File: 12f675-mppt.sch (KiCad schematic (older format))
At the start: 39 parts, among them IC1 PIC12F629-I/P, Q1 BUK9511-55A127, Q2 BUK9511-55A127, Q3 2N2222A, Q4 2N2222A, Q5 2N2907A, SW1 Write OP-AMP DIFF, U1 7805, U2 LM358N

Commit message: add PCB layout.
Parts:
- removed U1: 7805, symbol 12f675-mppt-rescue:7805
- added J1: S+, Connectors:1pin, symbol Connector:Conn_01x01_Male
- added J2: S-, Connectors:1pin, symbol Connector:Conn_01x01_Male
- added J3: O+, Connectors:1pin, symbol Connector:Conn_01x01_Male
- added J4: O-, Connectors:1pin, symbol Connector:Conn_01x01_Male
- added U1: LM7805_TO220, TO_SOT_Packages_THT:TO-220-3_Vertical, symbol Regulator_Linear:LM7805_TO220
- C1, C2, C3, C5, C7: footprint (none) -> Capacitors_THT:CP_Radial_D12.5mm_P5.00mm
- C4: footprint (none) -> Capacitors_THT:C_Disc_D7.5mm_W4.4mm_P5.00mm
- D1, D2, D6: footprint (none) -> Diodes_THT:D_DO-201AD_P15.24mm_Horizontal
- D3, D5: footprint (none) -> Diodes_THT:D_DO-41_SOD81_P10.16mm_Horizontal
- D4, D8, D9: footprint (none) -> LEDs:LED_D4.0mm
- IC1, U2: footprint (none) -> Housings_DIP:DIP-8_W7.62mm_LongPads
- L1: footprint (none) -> Inductors_THT:L_Toroid_Vertical_L33.0mm_W17.8mm_P12.70mm_Pulse_KM-5
- Q1, Q2: footprint (none) -> TO_SOT_Packages_THT:TO-220-3_Vertical
- Q3, Q4, Q5: footprint (none) -> TO_SOT_Packages_THT:TO-92_Inline_Wide
- R1, R10, R12, R13, R14, R15, R16, R2, R3, R4, R5, R6, R7, R8, R9: footprint (none) -> Resistors_THT:R_Axial_DIN0309_L9.0mm_D3.2mm_P12.70mm_Horizontal
- SW1: footprint (none) -> Buttons_Switches_THT:SW_PUSH_6mm
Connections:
- net labels added: +24V, GNDPWR, PRI_HI, PRI_LO
- net labels removed: L+, L-, S+, S-
- wire segments 148 -> 154

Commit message: Fix High-z turn on FET problem.
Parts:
- added R11: 10k, Resistors_THT:R_Axial_DIN0309_L9.0mm_D3.2mm_P12.70mm_Horizontal, symbol Device:R
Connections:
- net BootStrap: now also R11.1
- net at IC1.7 (CIN+/ICSPDAT/GP0), R7.2: now also R11.2
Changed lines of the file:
@@
 Sheet 1 1
 Title "Simple MPPT with 12F675 v5"
-Date "2019-01-11"
-Rev "1.6b"
+Date "2019-02-13"
+Rev "1.61"
 Comp ""
 Comment1 ""
@@
 	5850 2650 5850 2700
 Wire Wire Line
-	5250 3400 5450 3400
+	5250 3400 5300 3400
 Wire Wire Line
 	5450 3400 5450 3300
@@
 Connection ~ 5850 2350
 Wire Wire Line
-	5200 2350 3500 2350
+	5200 2350 5100 2350
 Wire Wire Line
 	6250 2700 6300 2700
@@
 Wire Wire Line
 	1200 1300 1350 1300
+$Comp
+L Device:R R11
+U 1 1 5C640CF9
+P 5100 2800
+F 0 "R11" V 5180 2800 50  0000 C CNN
+F 1 "10k" V 5100 2800 50  0000 C CNN
+F 2 "Resistors_THT:R_Axial_DIN0309_L9.0mm_D3.2mm_P12.70mm_Horizontal" V 5030 2800 30  0001 C CNN
+F 3 "" H 5100 2800 30  0000 C CNN
+	1    5100 2800
+	1    0    0    -1
+$EndComp
+Wire Wire Line
+	5300 3400 5300 2950
+Wire Wire Line
+	5300 2950 5100 2950
+Connection ~ 5300 3400
+Wire Wire Line
+	5300 3400 5450 3400
+Wire Wire Line
+	5100 2350 5100 2650
+Connection ~ 5100 2350
+Wire Wire Line
+	5100 2350 3500 2350
 $EndSCHEMATC

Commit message: Fix R1, R15 values.
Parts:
- R1: value 4.7k -> 10k
- R15: value 10k -> 4.7k
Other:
- note added: "R15 : 6A -> 3.3k"
- note removed: "R15 : 6A -> 4.7k, 3A -> 10k"
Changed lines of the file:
@@
 Sheet 1 1
 Title "Simple MPPT with 12F675 v5"
-Date "2019-02-13"
-Rev "1.61"
+Date "2019-02-15"
+Rev "1.62"
 Comp ""
 Comment1 ""
@@
 P 9200 4850
 F 0 "R1" V 9280 4850 50  0000 C CNN
-F 1 "4.7k" V 9200 4850 50  0000 C CNN
+F 1 "10k" V 9200 4850 50  0000 C CNN
 F 2 "Resistors_THT:R_Axial_DIN0309_L9.0mm_D3.2mm_P12.70mm_Horizontal" V 9130 4850 50  0001 C CNN
 F 3 "" H 9200 4850 50  0000 C CNN
@@
 P 9650 4300
 F 0 "R15" V 9730 4300 50  0000 C CNN
-F 1 "10k" V 9650 4300 50  0000 C CNN
+F 1 "4.7k" V 9650 4300 50  0000 C CNN
 F 2 "Resistors_THT:R_Axial_DIN0309_L9.0mm_D3.2mm_P12.70mm_Horizontal" V 9580 4300 50  0001 C CNN
 F 3 "" H 9650 4300 50  0000 C CNN
@@
 	4900 5600 5650 5600
 Text Notes 9850 4250 0    50   ~ 0
-R15 : 6A -> 4.7k, 3A -> 10k
+R15 : 6A -> 3.3k
 $Comp
 L power:+24V #PWR01

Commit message: Update current sensing resistors.
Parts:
- R15: value 4.7k -> 3.3k
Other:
- note added: "6A, R2 = R4 = 47k"
- note removed: "R15 : 6A -> 3.3k"
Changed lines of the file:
@@
 P 9650 4300
 F 0 "R15" V 9730 4300 50  0000 C CNN
-F 1 "4.7k" V 9650 4300 50  0000 C CNN
+F 1 "3.3k" V 9650 4300 50  0000 C CNN
 F 2 "Resistors_THT:R_Axial_DIN0309_L9.0mm_D3.2mm_P12.70mm_Horizontal" V 9580 4300 50  0001 C CNN
 F 3 "" H 9650 4300 50  0000 C CNN
@@
 	4900 5600 5650 5600
 Text Notes 9850 4250 0    50   ~ 0
-R15 : 6A -> 3.3k
+6A, R2 = R4 = 47k
 $Comp
 L power:+24V #PWR01

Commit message: Change circuit. Exchange GP0(Current Sensing) and GP2(PWM).
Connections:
- net PV-Current: now also IC1.7 (CIN+/ICSPDAT/GP0); no longer IC1.5 (T0CKI/INT/COUT/GP2)
- net at R11.2, R7.2: now also IC1.5 (T0CKI/INT/COUT/GP2); no longer IC1.7 (CIN+/ICSPDAT/GP0)
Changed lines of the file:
@@
 EESchema Schematic File Version 4
 LIBS:12f675-mppt-cache
-EELAYER 26 0
+EELAYER 29 0
 EELAYER END
 $Descr A4 11693 8268
 encoding utf-8
 Sheet 1 1
-Title "Simple MPPT with 12F675 v5"
-Date "2019-02-15"
-Rev "1.62"
+Title "Simple MPPT with 12F675 v6"
+Date "2019-05-20"
+Rev "1.7"
 Comp ""
 Comment1 ""
@@
 	5850 2650 5850 2700
 Wire Wire Line
-	5250 3400 5300 3400
-Wire Wire Line
-	5450 3400 5450 3300
-Wire Wire Line
 	5450 3000 5550 3000
 Wire Wire Line
@@
 	5900 5850 9800 5850
 Wire Wire Line
-	5250 3600 6100 3600
-Wire Wire Line
 	1850 4200 1850 5600
 Connection ~ 1850 5600
@@
 Wire Wire Line
 	6100 4750 6100 3600
-Connection ~ 6100 3600
 Wire Notes Line
 	5900 3500 5900 5850
@@
 $EndComp
 Wire Wire Line
-	5300 3400 5300 2950
-Wire Wire Line
 	5300 2950 5100 2950
-Connection ~ 5300 3400
-Wire Wire Line
-	5300 3400 5450 3400
 Wire Wire Line
 	5100 2350 5100 2650
@@
 Wire Wire Line
 	5100 2350 3500 2350
+Wire Wire Line
+	6100 3600 5750 3600
+Wire Wire Line
+	5750 3600 5750 3400
+Wire Wire Line
+	5750 3400 5250 3400
+Connection ~ 6100 3600
+Wire Wire Line
+	5300 2950 5300 3300
+Wire Wire Line
+	5300 3300 5450 3300
+Wire Wire Line
+	5650 3300 5650 3600
+Wire Wire Line
+	5650 3600 5250 3600
+Connection ~ 5450 3300
+Wire Wire Line
+	5450 3300 5650 3300
 $EndSCHEMATC

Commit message: Add FET protection zener diode.
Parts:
- added D7: 1N4733A 5.1V, Diode_THT:D_DO-41_SOD81_P10.16mm_Horizontal, symbol Device:D_Zener
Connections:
- net at Q2.1 (G), Q4.1 (E), Q5.1 (E): now also D7.1 (K)
- net at C2.2, D1.2 (A), Q2.3 (S)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: now also D7.2 (A)
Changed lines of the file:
@@
 EESchema Schematic File Version 4
-LIBS:12f675-mppt-cache
-EELAYER 29 0
+EELAYER 30 0
 EELAYER END
 $Descr A4 11693 8268
@@
 	7750 2200 7800 2200
 Wire Wire Line
-	7250 3500 7750 3500
+	7250 3500 7450 3500
 Wire Wire Line
 	5850 5600 5650 5600
@@
 Wire Wire Line
 	5450 3300 5650 3300
+$Comp
+L Device:D_Zener D7
+U 1 1 608BDF62
+P 7450 3300
+F 0 "D7" V 7404 3380 50  0000 L CNN
+F 1 "1N4733A 5.1V" V 7495 3380 50  0000 L CNN
+F 2 "Diode_THT:D_DO-41_SOD81_P10.16mm_Horizontal" H 7450 3300 50  0001 C CNN
+F 3 "~" H 7450 3300 50  0001 C CNN
+	1    7450 3300
+	0    1    1    0
+$EndComp
+Wire Wire Line
+	7450 3450 7450 3500
+Connection ~ 7450 3500
+Wire Wire Line
+	7450 3500 7750 3500
+Wire Wire Line
+	7450 3150 7450 3050
+Connection ~ 7450 3050
 $EndSCHEMATC

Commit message: R9 -> 2.2k
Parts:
- R9: value 10k -> 2.2k
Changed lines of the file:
@@
 Sheet 1 1
 Title "Simple MPPT with 12F675 v6"
-Date "2019-05-20"
-Rev "1.7"
+Date "2021-05-07"
+Rev "1.8"
 Comp ""
 Comment1 ""
@@
 P 5850 2500
 F 0 "R9" V 5930 2500 50  0000 C CNN
-F 1 "10k" V 5850 2500 50  0000 C CNN
+F 1 "2.2k" V 5850 2500 50  0000 C CNN
 F 2 "Resistors_THT:R_Axial_DIN0309_L9.0mm_D3.2mm_P12.70mm_Horizontal" V 5780 2500 30  0001 C CNN
 F 3 "" H 5850 2500 30  0000 C CNN

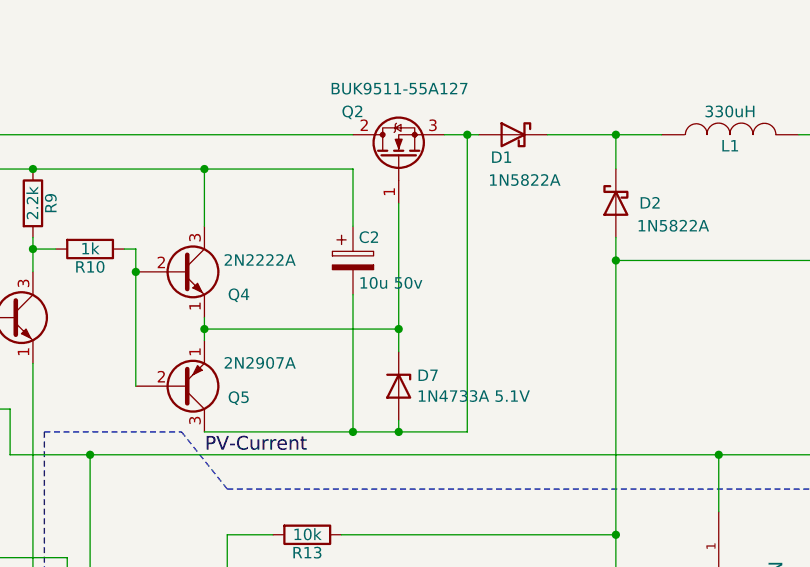
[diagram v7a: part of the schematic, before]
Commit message: C2 to 4.7uF.
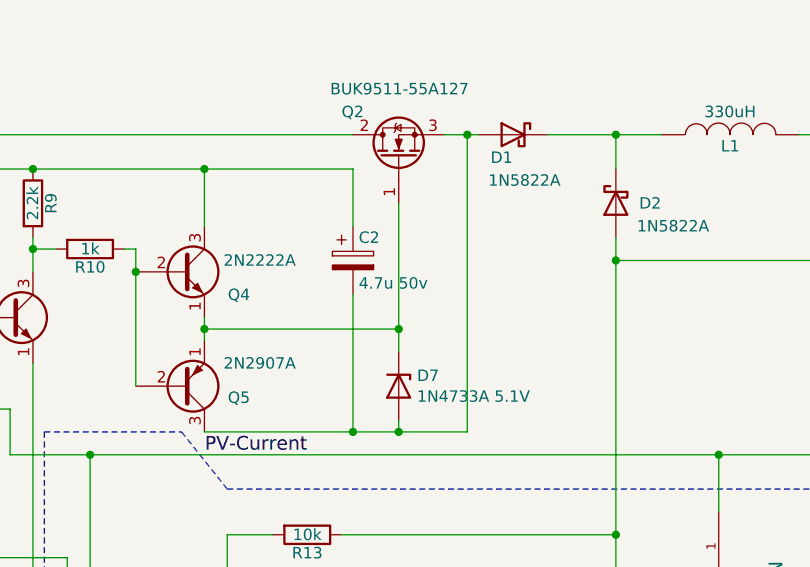
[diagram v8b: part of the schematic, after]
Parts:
- C2: value 10u 50v -> 4.7u 50v
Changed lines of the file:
@@
 P 7250 2750
 F 0 "C2" H 7275 2850 50  0000 L CNN
-F 1 "10u 50v" H 7275 2650 50  0000 L CNN
+F 1 "4.7u 50v" H 7275 2650 50  0000 L CNN
 F 2 "Capacitors_THT:CP_Radial_D12.5mm_P5.00mm" H 7288 2600 30  0001 C CNN
 F 3 "" H 7250 2750 60  0000 C CNN
